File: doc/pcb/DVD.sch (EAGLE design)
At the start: 45 parts, among them IC1 7805, IC2 74HC14N

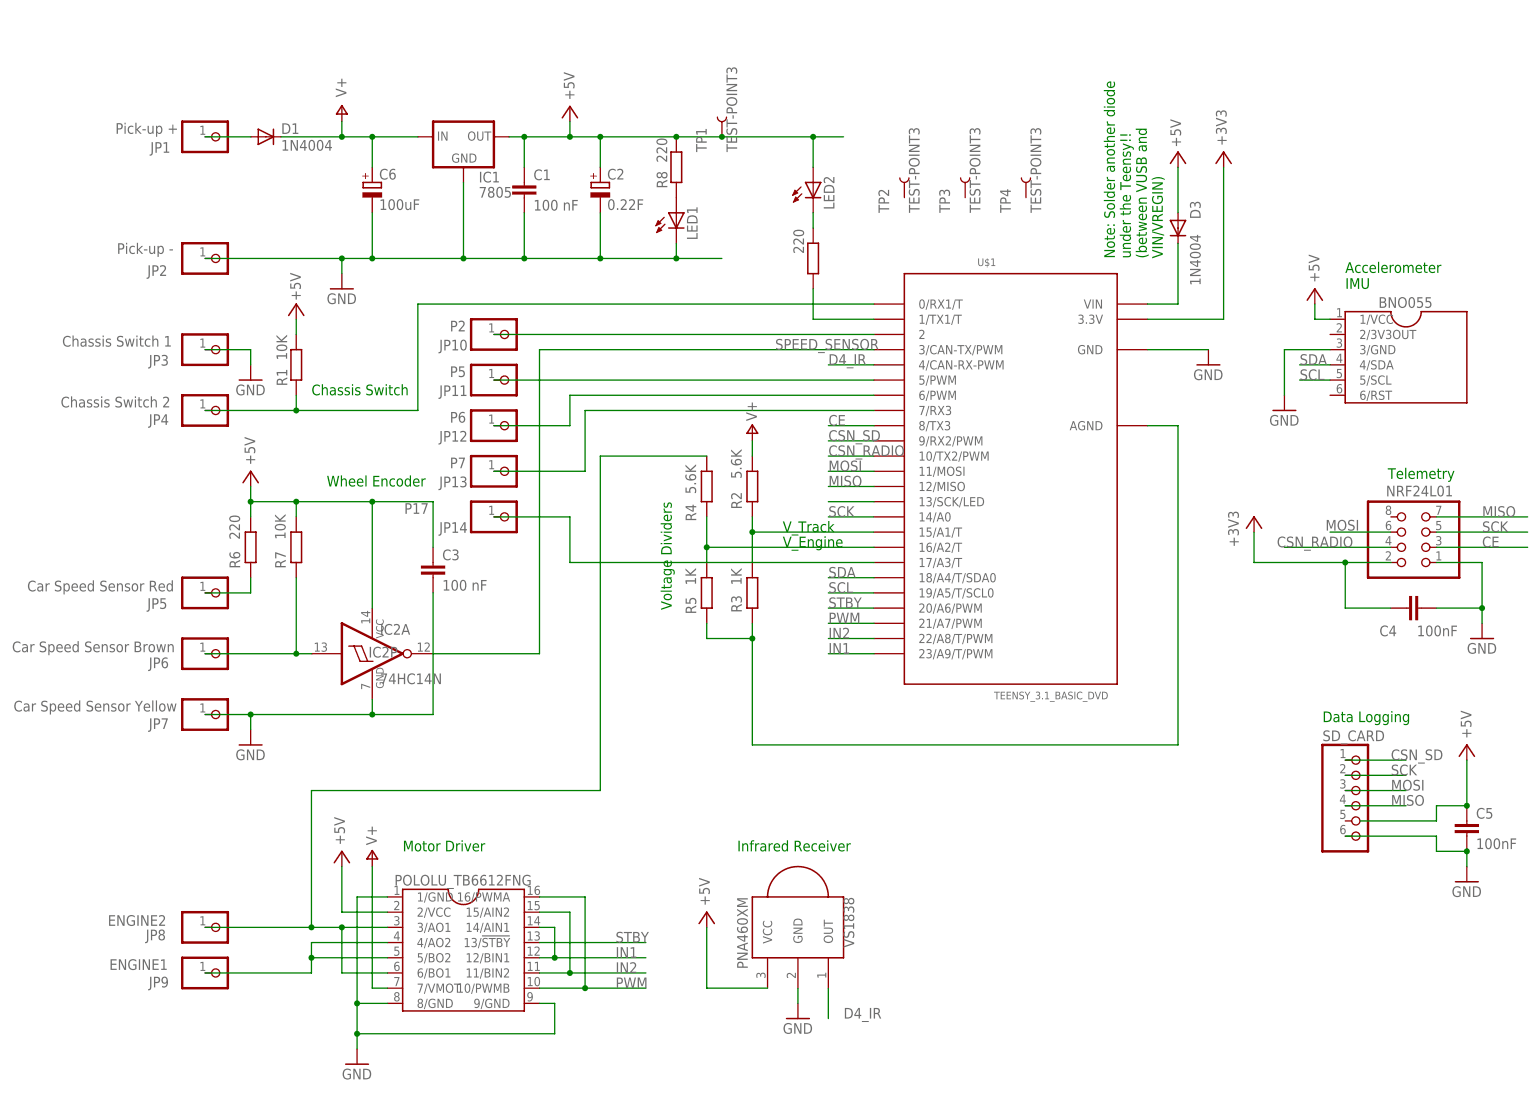
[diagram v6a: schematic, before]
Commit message: moved TPs, added Zener to ADC input
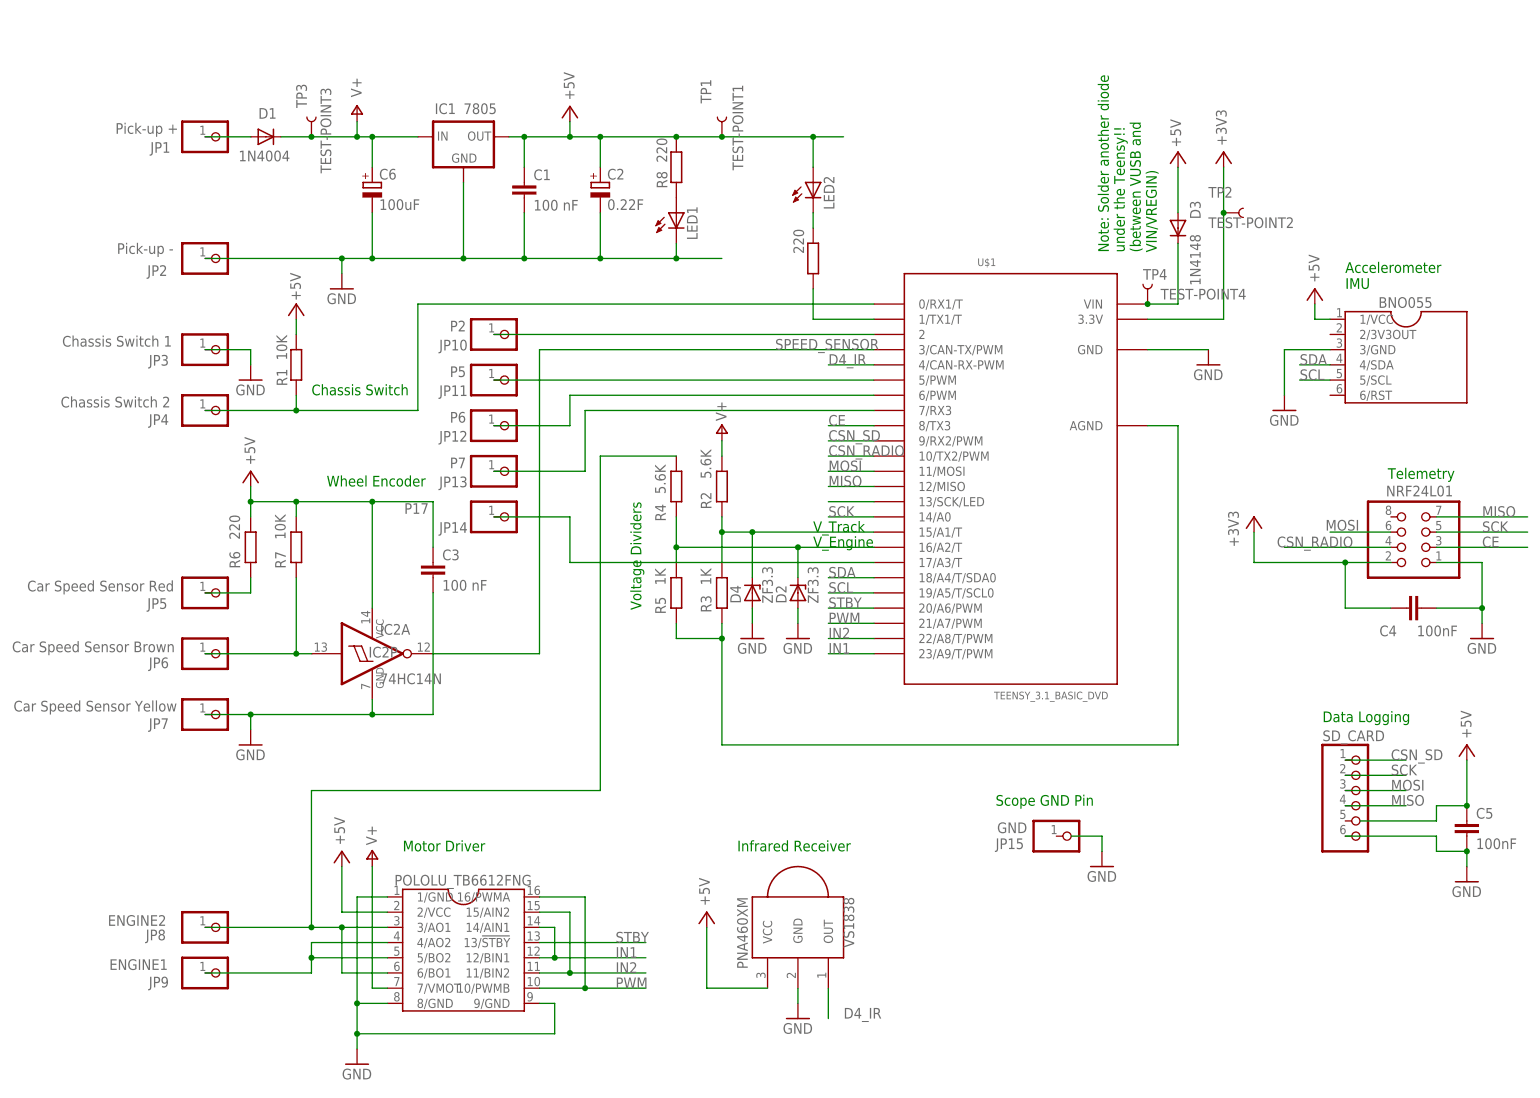
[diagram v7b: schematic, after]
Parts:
- added D2, D4: ZF3.3, diode:ZENER-DIODEZD-2.5
- added JP15: GND, pinhead:PINHD-1X1
- D3: value 1N4004 -> 1N4148
- TP1: value TEST-POINT3 -> TEST-POINT1
- TP2: value TEST-POINT3 -> TEST-POINT2
- TP4: value TEST-POINT3 -> TEST-POINT4
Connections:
- net +3V3: now also TP2.1
- net GND: now also D2.A, D4.A
- net N$1: now also TP4.1
- net N$10: now also D4.C
- net N$11: now also D2.C
- net V+: now also TP3.1
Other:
- note added: "Scope GND Pin"
- moved on the sheet: R2, R3, R4, R5, TP2, TP3, TP4

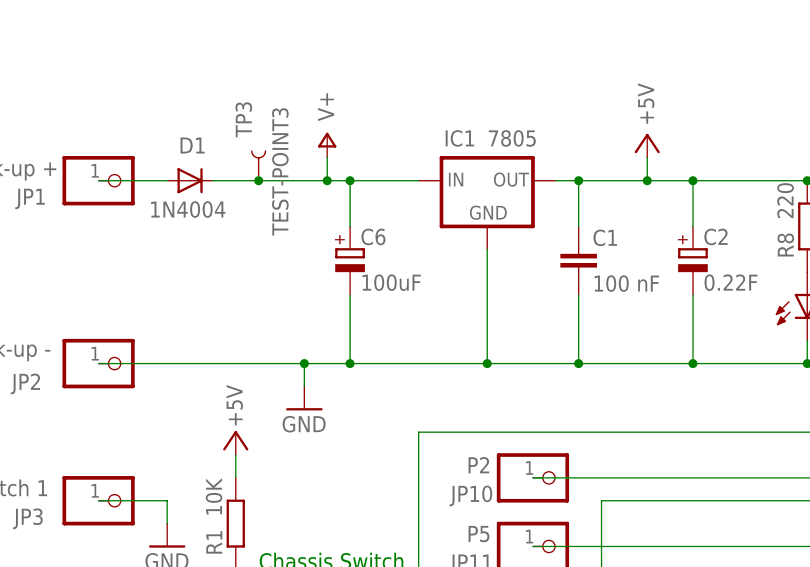
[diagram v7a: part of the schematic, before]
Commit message: Redid capacitor change
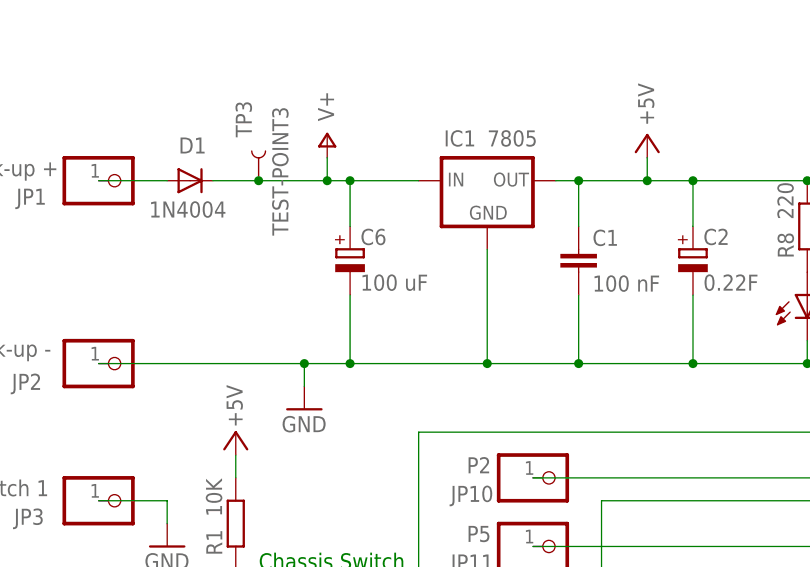
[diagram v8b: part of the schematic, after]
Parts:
- C6: value 100uF -> 100 uF; device resistor:CPOL-EUE15-6AXIAL -> rcl:CPOL-EUE2.5-6
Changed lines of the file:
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@@
 <part name="LED2" library="adafruit" deviceset="LED" device="5MM"/>
 <part name="C5" library="rcl" deviceset="C-EU" device="025-024X044" value="100nF"/>
-<part name="C6" library="resistor" deviceset="CPOL-EU" device="E15-6AXIAL" value="100uF"/>
 <part name="JP10" library="pinhead" deviceset="PINHD-1X1" device="" value="P2"/>
 <part name="JP11" library="pinhead" deviceset="PINHD-1X1" device="" value="P5"/>
@@
 <part name="GND9" library="supply1" deviceset="GND" device=""/>
 <part name="JP15" library="pinhead" deviceset="PINHD-1X1" device="" value="GND"/>
+<part name="C6" library="rcl" deviceset="CPOL-EU" device="E2.5-6" value="100 uF"/>
 </parts>
 <sheets>
@@
 <instance part="LED2" gate="G$1" x="96.52" y="147.32"/>
 <instance part="C5" gate="G$1" x="205.74" y="40.64"/>
-<instance part="C6" gate="G$1" x="22.86" y="147.32"/>
 <instance part="JP10" gate="G$1" x="45.72" y="121.92" smashed="yes">
 <attribute name="NAME" x="34.036" y="119.253" size="1.778" layer="95"/>
@@
 <attribute name="VALUE" x="127.254" y="38.608" size="1.778" layer="96"/>
 </instance>
+<instance part="C6" gate="G$1" x="22.86" y="147.32"/>
 </instances>
 <busses>
@@
 <wire x1="20.32" y1="157.48" x2="20.32" y2="154.94" width="0.1524" layer="91"/>
 <junction x="20.32" y="154.94"/>
-<pinref part="C6" gate="G$1" pin="+"/>
 <wire x1="22.86" y1="149.86" x2="22.86" y2="154.94" width="0.1524" layer="91"/>
 <junction x="22.86" y="154.94"/>
 <pinref part="TP3" gate="G$1" pin="1"/>
 <junction x="12.7" y="154.94"/>
+<pinref part="C6" gate="G$1" pin="+"/>
 </segment>
 </net>
@@
 <wire x1="60.96" y1="142.24" x2="60.96" y2="134.62" width="0.1524" layer="91"/>
 <junction x="60.96" y="134.62"/>
-<pinref part="C6" gate="G$1" pin="-"/>
 <wire x1="22.86" y1="142.24" x2="22.86" y2="134.62" width="0.1524" layer="91"/>
 <junction x="22.86" y="134.62"/>
+<pinref part="C6" gate="G$1" pin="-"/>
 </segment>
 <segment>
